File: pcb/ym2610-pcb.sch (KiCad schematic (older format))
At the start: 132 parts, among them J1 MIDI_IN, J2 LINE_OUT, J3 HEADPHONES, J4 SPDIF_COAX, J5 UART, SW1 BTN_A, SW2 BTN_B, SW3 CRESET, U1 YM2610, U10 TSV914IPT, U11 TSV914IPT, U12 AD8532, U13 74LVC2G08, U14 74AHCT595, U15 74AHCT595, U16 SPDIF_OPTICAL, U17 74HCT573, U18 TLP2361, U19 74HCT153, U2 YM3016, U20 74HCT153, U21 74LVC257, U3 74LV1T34, U4 74LVC244, U5 74LV1T34, U6 74HCT573, U7 74HCT573, U8 74HCT153, U9 74HCT153

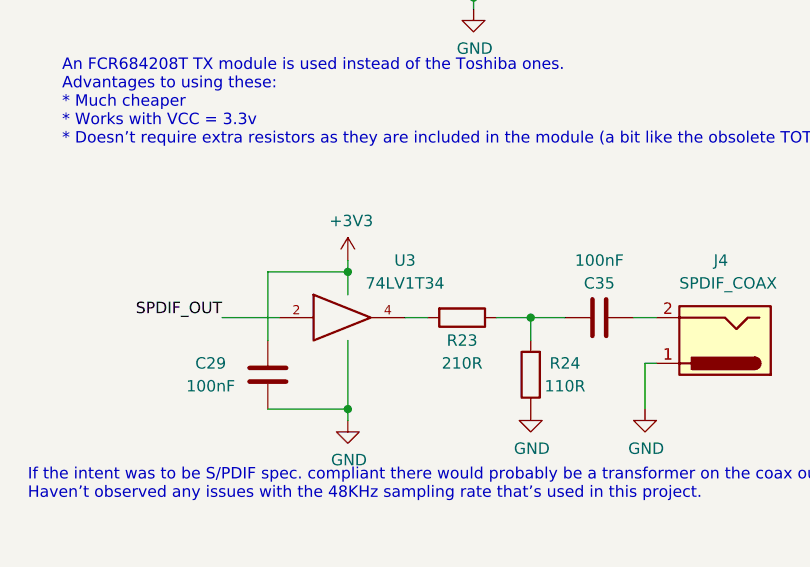
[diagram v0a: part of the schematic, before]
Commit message: pcb: replace LV1T34 with LVC1G34 as S/PDIF coax buffer
The earlier design used the LVC part but to remove a unique item from BOM, it was replaced with another LV1 part. This was a mistake as the LV1T34 can't quite drive the coax load (vs. 24mA on the LVC1G34).
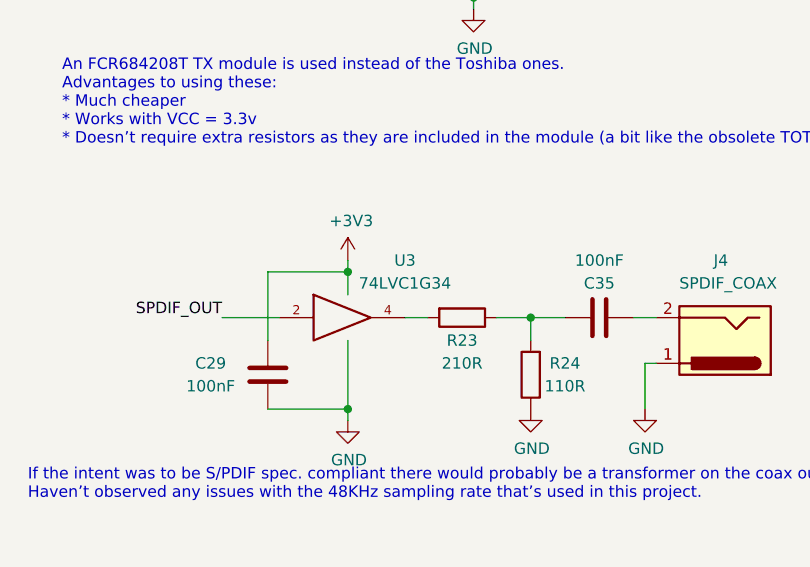
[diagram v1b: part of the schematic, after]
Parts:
- U3: value 74LV1T34 -> 74LVC1G34; footprint Package_TO_SOT_SMD:SOT-23-5 -> Package_TO_SOT_SMD:SOT-353_SC-70-5
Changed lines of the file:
@@
 P 6250 13650
 F 0 "U3" H 6500 13900 50  0000 C CNN
-F 1 "74LV1T34" H 6500 13800 50  0000 C CNN
-F 2 "Package_TO_SOT_SMD:SOT-23-5" H 6250 13650 50  0001 C CNN
+F 1 "74LVC1G34" H 6500 13800 50  0000 C CNN
+F 2 "Package_TO_SOT_SMD:SOT-353_SC-70-5" H 6250 13650 50  0001 C CNN
 F 3 "" H 6250 13650 50  0001 C CNN
 	1    6250 13650

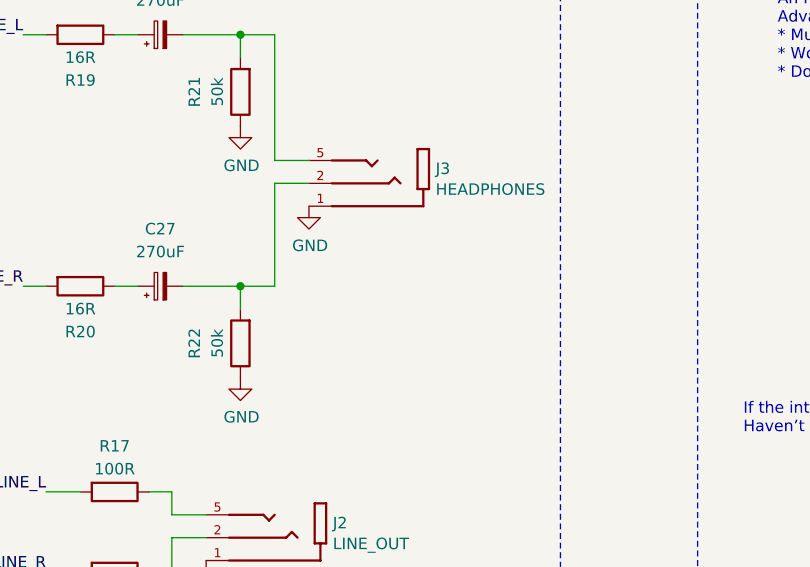
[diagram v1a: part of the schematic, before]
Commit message: pcb: misc. cleanup in analog section
* added net-tie and dedicated return for headphone to avoid running over much of the DAC circuit
* route SSG on back layer
* ground fill on top
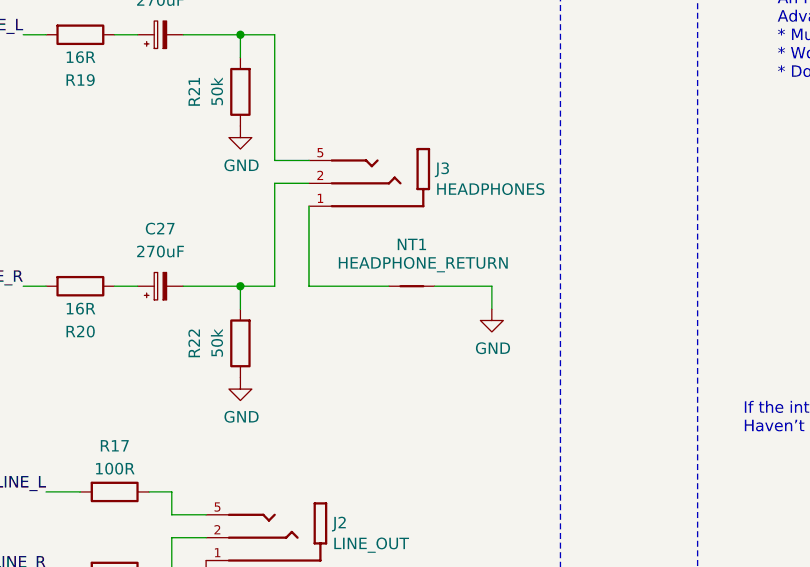
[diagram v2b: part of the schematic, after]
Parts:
- added NT1: HEADPHONE_RETURN, NetTie:NetTie-2_SMD_Pad0.5mm, symbol Device:Net-Tie_2
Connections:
- net GND: now also NT1.2; no longer J3.1
- new net: J3.1, NT1.1
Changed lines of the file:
@@
 	2800 13250 2950 13250
-$Comp
-L power:GND #PWR0130
-U 1 1 60474176
-P 2950 13450
-F 0 "#PWR0130" H 2950 13200 50  0001 C CNN
-F 1 "GND" H 2955 13277 50  0000 C CNN
-F 2 "" H 2950 13450 50  0001 C CNN
-F 3 "" H 2950 13450 50  0001 C CNN
-	1    2950 13450
-	1    0    0    -1
-$EndComp
 $Comp
 L Device:CP_Small C27
@@
 Wire Notes Line
 	8200 9600 10250 9600
+$Comp
+L Device:Net-Tie_2 NT1
+U 1 1 60723D00
+P 3400 13800
+F 0 "NT1" H 3400 13981 50  0000 C CNN
+F 1 "HEADPHONE_RETURN" H 3450 13900 50  0000 C CNN
+F 2 "NetTie:NetTie-2_SMD_Pad0.5mm" H 3400 13800 50  0001 C CNN
+F 3 "~" H 3400 13800 50  0001 C CNN
+	1    3400 13800
+	1    0    0    -1
+$EndComp
+Wire Wire Line
+	2950 13450 2950 13800
+Wire Wire Line
+	2950 13800 3300 13800
+$Comp
+L power:GND #PWR0130
+U 1 1 60474176
+P 3750 13900
+F 0 "#PWR0130" H 3750 13650 50  0001 C CNN
+F 1 "GND" H 3755 13727 50  0000 C CNN
+F 2 "" H 3750 13900 50  0001 C CNN
+F 3 "" H 3750 13900 50  0001 C CNN
+	1    3750 13900
+	1    0    0    -1
+$EndComp
+Wire Wire Line
+	3500 13800 3750 13800
+Wire Wire Line
+	3750 13800 3750 13900
 $EndSCHEMATC

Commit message: sch: added rev. text
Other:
- note added: "By Dan Rodrigues\n\nhttps://github.com/dan-rodrigues"
- note added: "YM2610 PCB"
- note added: "v1.0.1"
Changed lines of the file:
@@
 Wire Wire Line
 	3750 13800 3750 13900
+Text Notes 19030 15780 0    79   Italic 16
+YM2610 PCB
+Text Notes 22270 15910 0    50   Italic 10
+v1.0.1
+Text Notes 18690 15370 0    50   ~ 0
+By Dan Rodrigues\n\nhttps://github.com/dan-rodrigues
 $EndSCHEMATC

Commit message: pcb / sch: added CERL-OHL license
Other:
- note added: "By Dan Rodrigues\nhttps://github.com/dan-rodrigues\n\nLicensed under CERN-OHL-W-2.0"
- note removed: "By Dan Rodrigues\n\nhttps://github.com/dan-rodrigues"
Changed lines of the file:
@@
 v1.0.1
 Text Notes 18690 15370 0    50   ~ 0
-By Dan Rodrigues\n\nhttps://github.com/dan-rodrigues
+By Dan Rodrigues\nhttps://github.com/dan-rodrigues\n\nLicensed under CERN-OHL-W-2.0
 $EndSCHEMATC

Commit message: pcb: tentative v1.0.1
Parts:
- added C52: 150uF, Capacitor_SMD:CP_Elec_5x5.8, symbol Device:CP
- added NT2: DAC_CAP_NT, NetTie:NetTie-2_SMD_Pad0.5mm, symbol Device:Net-Tie_2
- added R28, R29, R30, R31, R32: 100R, Resistor_SMD:R_0603_1608Metric, symbol Device:R
- R21, R22: value 50k -> 47k
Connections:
- net +5V: now also RN4.1 (R1.1), RN4.2 (R2.1), RN4.3 (R3.1), RN4.4 (R4.1)
- net +5VA: now also R28.2; no longer C4.2, C50.2, RN4.1 (R1.1), RN4.2 (R2.1), RN4.3 (R3.1), RN4.4 (R4.1), U2.1 (VDD), U2.3 (VDD), U2.6 (FORM)
- net DAC_CLK: now also R29.2; no longer U2.5 (CLK)
- net DAC_SH1: now also R31.2; no longer U2.8 (SAM1)
- net DAC_SH2: now also R32.2; no longer U2.7 (SAM2)
- net DAC_SO: now also R30.2; no longer U2.4 (SD)
- net GND: now also NT2.2
- new net: R30.1, U2.4 (SD)
- new net: R29.1, U2.5 (CLK)
- new net: R32.1, U2.7 (SAM2)
- new net: R31.1, U2.8 (SAM1)
- new net: C52.2, NT2.1
- new net DAC_5V: C4.2, C50.2, C52.1, R28.1, U2.1 (VDD), U2.3 (VDD), U2.6 (FORM)
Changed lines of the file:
@@
 	1    0    0    -1
 $EndComp
-Text Label 2550 1550 2    50   ~ 0
+Text Label 2150 1550 2    50   ~ 0
 DAC_CLK
-Text Label 2550 1750 2    50   ~ 0
+Text Label 2150 1750 2    50   ~ 0
 DAC_SH1
-Text Label 2550 1850 2    50   ~ 0
+Text Label 2150 1850 2    50   ~ 0
 DAC_SH2
-Text Label 2550 1650 2    50   ~ 0
+Text Label 2150 1650 2    50   ~ 0
 DAC_SO
 $Comp
@@
 	3250 1250 3250 1350
 Connection ~ 3150 1250
-$Comp
-L power:+5VA #PWR0110
-U 1 1 600B82DD
-P 3150 1150
-F 0 "#PWR0110" H 3150 1000 50  0001 C CNN
-F 1 "+5VA" H 3165 1323 50  0000 C CNN
-F 2 "" H 3150 1150 50  0001 C CNN
-F 3 "" H 3150 1150 50  0001 C CNN
-	1    3150 1150
-	1    0    0    -1
-$EndComp
 Wire Wire Line
 	3150 1150 3150 1250
@@
 U 1 1 6146A7DF
 P 2650 12950
-F 0 "R21" V 2850 12950 50  0000 C CNN
-F 1 "50k" V 2750 12950 50  0000 C CNN
+F 0 "R21" H 2780 12900 50  0000 C CNN
+F 1 "47k" H 2780 13000 50  0000 C CNN
 F 2 "Resistor_SMD:R_0603_1608Metric" V 2580 12950 50  0001 C CNN
 F 3 "~" H 2650 12950 50  0001 C CNN
@@
 U 1 1 603B89B6
 P 2650 14050
-F 0 "R22" V 2850 14050 50  0000 C CNN
-F 1 "50k" V 2750 14050 50  0000 C CNN
+F 0 "R22" H 2780 14000 50  0000 C CNN
+F 1 "47k" H 2780 14100 50  0000 C CNN
 F 2 "Resistor_SMD:R_0603_1608Metric" V 2580 14050 50  0001 C CNN
 F 3 "~" H 2650 14050 50  0001 C CNN
@@
 Connection ~ 7250 2550
 Connection ~ 7250 2700
-$Comp
-L power:+5VA #PWR0185
-U 1 1 6067915E
-P 7250 3350
-F 0 "#PWR0185" H 7250 3200 50  0001 C CNN
-F 1 "+5VA" H 7265 3523 50  0000 C CNN
-F 2 "" H 7250 3350 50  0001 C CNN
-F 3 "" H 7250 3350 50  0001 C CNN
-	1    7250 3350
-	1    0    0    -1
-$EndComp
 Text Label 20300 11400 2    50   ~ 0
 RMPX_3V3
@@
 DAC (FM / Digital sound sources only)\nSSG analog (YM2149) is output direct from YM2610
 Wire Notes Line
-	2000 3750 2000 650
-Wire Notes Line
-	2000 650  5650 650
-Wire Notes Line
 	5650 650  5650 3750
 Wire Notes Line
-	5650 3750 2000 3750
+	5650 3750 600  3750
 Text Notes 12850 13000 0    50   ~ 0
 YM2610 PCM input latches
@@
 Text Notes 18690 15370 0    50   ~ 0
 By Dan Rodrigues\nhttps://github.com/dan-rodrigues\n\nLicensed under CERN-OHL-W-2.0
+$Comp
+L Device:CP C52
+U 1 1 606538A2
+P 1550 2800
+F 0 "C52" H 1650 2850 50  0000 L CNN
+F 1 "150uF" H 1650 2750 50  0000 L CNN
+F 2 "Capacitor_SMD:CP_Elec_5x5.8" H 1588 2650 50  0001 C CNN
+F 3 "~" H 1550 2800 50  0001 C CNN
+F 4 "10v" H 1550 2800 50  0001 C CNN "Voltage"
+	1    1550 2800
+	1    0    0    -1
+$EndComp
+$Comp
+L Device:R R28
+U 1 1 60655CD6
+P 1240 2600
+F 0 "R28" V 1340 2610 50  0000 C CNN
+F 1 "100R" V 1440 2610 50  0000 C CNN
+F 2 "Resistor_SMD:R_0603_1608Metric" V 1170 2600 50  0001 C CNN
+F 3 "~" H 1240 2600 50  0001 C CNN
+	1    1240 2600
+	0    1    1    0
+$EndComp
+$Comp
+L power:GND #PWR04
+U 1 1 6065730C
+P 1550 3350
+F 0 "#PWR04" H 1550 3100 50  0001 C CNN
+F 1 "GND" H 1555 3177 50  0000 C CNN
+F 2 "" H 1550 3350 50  0001 C CNN
+F 3 "" H 1550 3350 50  0001 C CNN
+	1    1550 3350
+	1    0    0    -1
+$EndComp
+$Comp
+L Device:Net-Tie_2 NT2
+U 1 1 60660D81
+P 1550 3150
+F 0 "NT2" V 1504 3194 50  0000 L CNN
+F 1 "DAC_CAP_NT" V 1595 3194 50  0000 L CNN
+F 2 "NetTie:NetTie-2_SMD_Pad0.5mm" H 1550 3150 50  0001 C CNN
+F 3 "~" H 1550 3150 50  0001 C CNN
+	1    1550 3150
+	0    1    1    0
+$EndComp
+Text Label 1750 2600 0    50   ~ 0
+DAC_5V
+$Comp
+L power:+5VA #PWR03
+U 1 1 60666069
+P 950 2500
+F 0 "#PWR03" H 950 2350 50  0001 C CNN
+F 1 "+5VA" H 965 2673 50  0000 C CNN
+F 2 "" H 950 2500 50  0001 C CNN
+F 3 "" H 950 2500 50  0001 C CNN
+	1    950  2500
+	1    0    0    -1
+$EndComp
+Wire Wire Line
+	950  2500 950  2600
+Wire Wire Line
+	1550 2600 1550 2650
+Wire Wire Line
+	950  2600 1090 2600
+Wire Wire Line
+	1390 2600 1550 2600
+Wire Wire Line
+	1550 2600 1750 2600
+Connection ~ 1550 2600
+Wire Wire Line
+	1550 2950 1550 3050
+Wire Wire Line
+	1550 3250 1550 3350
+Text Label 3150 1150 1    50   ~ 0
+DAC_5V
+Wire Notes Line
+	600  3750 600  650
+Wire Notes Line
+	600  650  5650 650
+$Comp
+L Device:R R29
+U 1 1 610FB61C
+P 2400 1550
+F 0 "R29" V 1950 1550 50  0000 C CNN
+F 1 "100R" V 2400 1550 50  0000 C CNN
+F 2 "Resistor_SMD:R_0603_1608Metric" V 2330 1550 50  0001 C CNN
+F 3 "~" H 2400 1550 50  0001 C CNN
+	1    2400 1550
+	0    1    1    0
+$EndComp
+$Comp
+L Device:R R30
+U 1 1 610FCC10
+P 2400 1650
+F 0 "R30" V 1950 1650 50  0000 C CNN
+F 1 "100R" V 2400 1650 50  0000 C CNN
+F 2 "Resistor_SMD:R_0603_1608Metric" V 2330 1650 50  0001 C CNN
+F 3 "~" H 2400 1650 50  0001 C CNN
+	1    2400 1650
+	0    1    1    0
+$EndComp
+$Comp
+L Device:R R31
+U 1 1 610FCEE1
+P 2400 1750
+F 0 "R31" V 1950 1750 50  0000 C CNN
+F 1 "100R" V 2400 1750 50  0000 C CNN
+F 2 "Resistor_SMD:R_0603_1608Metric" V 2330 1750 50  0001 C CNN
+F 3 "~" H 2400 1750 50  0001 C CNN
+	1    2400 1750
+	0    1    1    0
+$EndComp
+$Comp
+L Device:R R32
+U 1 1 610FD4FA
+P 2400 1850
+F 0 "R32" V 1950 1850 50  0000 C CNN
+F 1 "100R" V 2400 1850 50  0000 C CNN
+F 2 "Resistor_SMD:R_0603_1608Metric" V 2330 1850 50  0001 C CNN
+F 3 "~" H 2400 1850 50  0001 C CNN
+	1    2400 1850
+	0    1    1    0
+$EndComp
+Wire Wire Line
+	2250 1550 2150 1550
+Wire Wire Line
+	2150 1650 2250 1650
+Wire Wire Line
+	2250 1750 2150 1750
+Wire Wire Line
+	2150 1850 2250 1850
+$Comp
+L power:+5V #PWR0110
+U 1 1 618D7ECF
+P 7250 3350
+F 0 "#PWR0110" H 7250 3200 50  0001 C CNN
+F 1 "+5V" H 7265 3523 50  0000 C CNN
+F 2 "" H 7250 3350 50  0001 C CNN
+F 3 "" H 7250 3350 50  0001 C CNN
+	1    7250 3350
+	1    0    0    -1
+$EndComp
+$Comp
+L power:PWR_FLAG #FLG0103
+U 1 1 606CCBCD
+P 1550 2450
+F 0 "#FLG0103" H 1550 2525 50  0001 C CNN
+F 1 "PWR_FLAG" H 1550 2623 50  0000 C CNN
+F 2 "" H 1550 2450 50  0001 C CNN
+F 3 "~" H 1550 2450 50  0001 C CNN
+	1    1550 2450
+	1    0    0    -1
+$EndComp
+Wire Wire Line
+	1550 2450 1550 2600
 $EndSCHEMATC

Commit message: pcb: v1.1.0
* Layout cleanup and removal of now-redundant parts
* Fixed lots of plane breakage near center of board
* Added 47pF caps to RMPX/PMPX
* Updated .pcf with reassigned pins
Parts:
- removed RN1, RN10, RN2, RN3, RN4, RN5, RN6, RN7, RN8, RN9: 100k, Resistor_SMD:R_Array_Convex_4x0603, symbol Device:R_Pack04
- removed RN11, RN14: 100R, Resistor_SMD:R_Array_Convex_4x0603, symbol Device:R_Pack04
- removed U4: 74LVC244, Package_SO:TSSOP-20_4.4x6.5mm_P0.65mm, symbol 74xx:74HC244
- added C53: 10uF, Capacitor_SMD:C_0603_1608Metric, symbol Device:C
- added C54, C55: 47pF, Capacitor_SMD:C_0603_1608Metric, symbol Device:C
- added R33, R34, R35, R36, R37, R38: 100R, Resistor_SMD:R_0603_1608Metric, symbol Device:R
- added R39, R40, R41, R42, R43, R44, R45, R46, R47, R48, R49, R50, R51, R52, R53, R54, R55, R56, R57, R58, R59, R60, R61, R62, R63, R64: 100k, Resistor_SMD:R_0603_1608Metric, symbol Device:R
- added TP1, TP2, TP3, TP4, TP5: TestPoint, TestPoint:TestPoint_Pad_D1.0mm, symbol Connector:TestPoint
- added U4: 74LVCH245, Package_SO:TSSOP-20_4.4x6.5mm_P0.65mm, symbol 74xx:74LS245
- renumbered RN12 to RN1, RN13 to RN2
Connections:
- net +3V3: now also C53.2, U4.1 (A->B), U4.20 (VCC)
- net +5V: now also R39.1, R40.1, R41.1, R42.1, R43.1, R44.1, R45.1, R46.1, R47.1, R48.1, R49.1, R50.1, R51.1, R52.1, R53.1, R54.1, R55.1, R56.1, R57.1, R58.1, R59.1, R60.1, R61.1, R62.1, R63.1, R64.1; no longer U17.6 (D4), U17.7 (D5), U17.8 (D6), U17.9 (D7)
- net BTN_A: now also R38.2
- net BTN_B: now also R37.2
- net DAC_CLK: now also U4.4 (A2)
- net DAC_CLK_3V3: now also A1.7 (P5), RN2.8 (R1.2); no longer A1.13 (P11), RN2.6 (R3.2)
- net DAC_SH1: now also U4.2 (A0)
- net DAC_SH1_3V3: now also A1.22 (P20), R33.1; no longer A1.14 (P12), RN2.5 (R4.2)
- net DAC_SH2: now also U4.3 (A1)
- net DAC_SH2_3V3: now also A1.21 (P19), R34.1; no longer A1.22 (P20)
- net DAC_SO: now also U4.5 (A3)
- net DAC_SO_3V3: now also A1.8 (P6), RN2.7 (R2.2); no longer A1.21 (P19)
- net GND: now also U17.6 (D4), U17.7 (D5), U17.8 (D6), U17.9 (D7), C53.1, C54.1, C55.1, TP1.1, TP2.1, TP3.1, TP4.1, TP5.1, U4.10 (GND), U4.19 (CE), U4.8 (A6), U4.9 (A7)
- net PA10: now also R63.2
- net PA11: now also R64.2
- net PA8: now also R61.2
- net PA9: now also R62.2
- net PAD0: now also R39.2
- net PAD1: now also R40.2
- net PAD2: now also R41.2
- net PAD3: now also R42.2
- net PAD4: now also R43.2
- net PAD5: now also R44.2
- net PAD6: now also R45.2
- net PAD7: now also R46.2
- net PMPX: now also C55.2, U4.7 (A5)
- net PMPX_3V3: now also A1.10 (P8), RN2.5 (R4.2); no longer A1.12 (P10), RN2.7 (R2.2)
- net RA20: now also R57.2
- net RA21: now also R58.2
- net RA22: now also R59.2
- net RA23: now also R60.2
- net RA8: now also R55.2
- net RA9: now also R56.2
- net RAD0: now also U6.12 (Q7), R47.2; no longer U6.19 (Q0)
- net RAD1: now also U6.13 (Q6), R48.2; no longer U6.18 (Q1)
- net RAD2: now also U6.14 (Q5), R49.2; no longer U6.17 (Q2)
- net RAD3: now also U6.15 (Q4), R50.2; no longer U6.16 (Q3)
- net RAD4: now also U6.16 (Q3), R51.2; no longer U6.15 (Q4)
- net RAD5: now also U6.17 (Q2), R52.2; no longer U6.14 (Q5)
- net RAD6: now also U6.18 (Q1), R53.2; no longer U6.13 (Q6)
- net RAD7: now also U6.19 (Q0), R54.2; no longer U6.12 (Q7)
- net RMPX: now also C54.2, U4.6 (A4)
- net RMPX_3V3: now also A1.9 (P7), RN2.6 (R3.2); no longer A1.11 (P9), RN2.8 (R1.2)
- net UART_RX: now also R35.1
- net UART_TX: now also R36.1
- net YM_IO_0: now also RN1.5 (R4.2), U21.4 (Za), U6.2 (D0); no longer A1.7 (P5), RN1.8 (R1.2), U6.6 (D4)
- net YM_IO_1: now also RN1.6 (R3.2), U21.7 (Zb), U6.3 (D1); no longer A1.8 (P6), RN1.7 (R2.2), U6.7 (D5)
- net YM_IO_2: now also RN1.7 (R2.2), U21.12 (Zc), U6.4 (D2); no longer A1.9 (P7), RN1.6 (R3.2), U6.8 (D6)
- net YM_IO_3: now also RN1.8 (R1.2), U21.9 (Zd), U6.5 (D3); no longer A1.10 (P8), RN1.5 (R4.2), U6.9 (D7)
- net at RN2.4 (R4.1): now also U4.13 (B5)
- net at RN2.3 (R3.1): now also U4.14 (B4)
- net at RN2.2 (R2.1): now also U4.15 (B3)
- net at RN2.1 (R1.1): now also U4.16 (B2)
- net at U17.19 (Q0), U7.2 (D0): now also U6.9 (D7); no longer U6.2 (D0)
- net at U17.18 (Q1), U7.3 (D1): now also U6.8 (D6); no longer U6.3 (D1)
- net at U17.17 (Q2), U7.4 (D2): now also U6.7 (D5); no longer U6.4 (D2)
- net at U17.16 (Q3), U7.5 (D3): now also U6.6 (D4); no longer U6.5 (D3)
- net at RN1.3 (R3.1): now also A1.13 (P11); no longer U21.12 (Zc)
- net at RN1.1 (R1.1): now also A1.11 (P9); no longer U21.4 (Za)
- net at RN1.2 (R2.1): now also A1.12 (P10); no longer U21.7 (Zb)
- net at RN1.4 (R4.1): now also A1.14 (P12); no longer U21.9 (Zd)
- net at SW1.1 (A): now also R38.1
- net at SW2.1 (A): now also R37.1
- net UART_RX_HEADER: no longer names the net of J5.2 (Pin_2)
- net UART_RX_HEADER: now also R35.2
- net UART_TX_HEADER: no longer names the net of J5.3 (Pin_3)
- net UART_TX_HEADER: now also R36.2
- new net: R34.2, U4.17 (B1)
- new net: R33.2, U4.18 (B0)
- no-connect marks 29 -> 21
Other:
- note added: "Pullups for YM2610 outputs to HCT153"
- note added: "v1.1.0"
- note removed: "Pullups for socketed components (YM2610 / YM3016)"
- note removed: "v1.0.1"
- moved on the sheet: J5, RN1, RN2
